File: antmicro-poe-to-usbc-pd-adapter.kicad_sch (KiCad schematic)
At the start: 0 parts

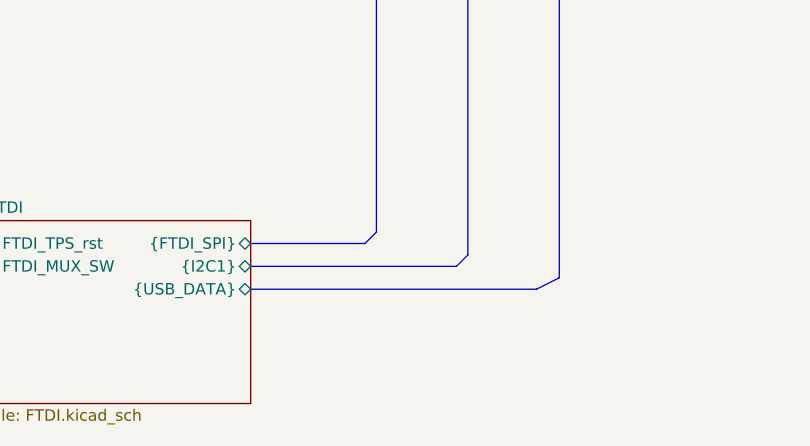
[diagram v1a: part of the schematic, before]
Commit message: [#62835] Tacle ERC problems, add PWR flags
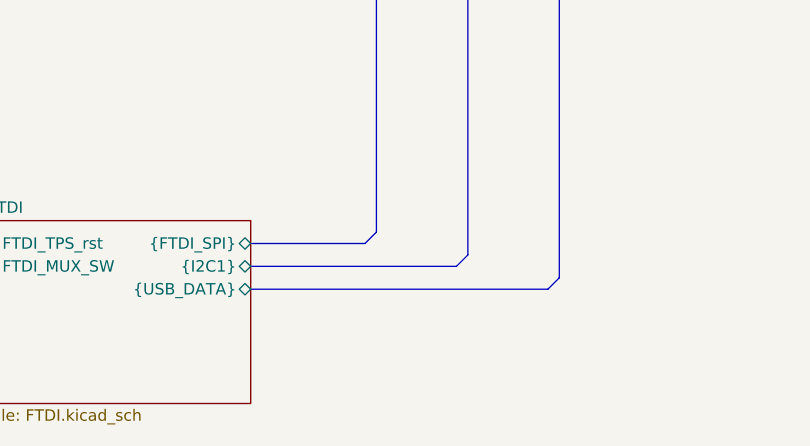
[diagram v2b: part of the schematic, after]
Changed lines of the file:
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@@
   (junction (at 232.41 111.76) (diameter 0) (color 0 0 0 0)
-  )
-  (bus (pts (xy 208.28 166.37) (xy 240.03 166.37))
-    (stroke (width 0) (type default))
   )
   (wire (pts (xy 173.99 124.46) (xy 179.07 124.46))
@@
     (stroke (width 0) (type default))
   )
-  (bus (pts (xy 240.03 166.37) (xy 242.57 165.1))
+  (bus (pts (xy 241.3 166.37) (xy 242.57 165.1))
     (stroke (width 0) (type default))
   )
@@
     (stroke (width 0) (type default))
   )
+  (bus (pts (xy 208.28 166.37) (xy 241.3 166.37))
+    (stroke (width 0) (type default))
+  )

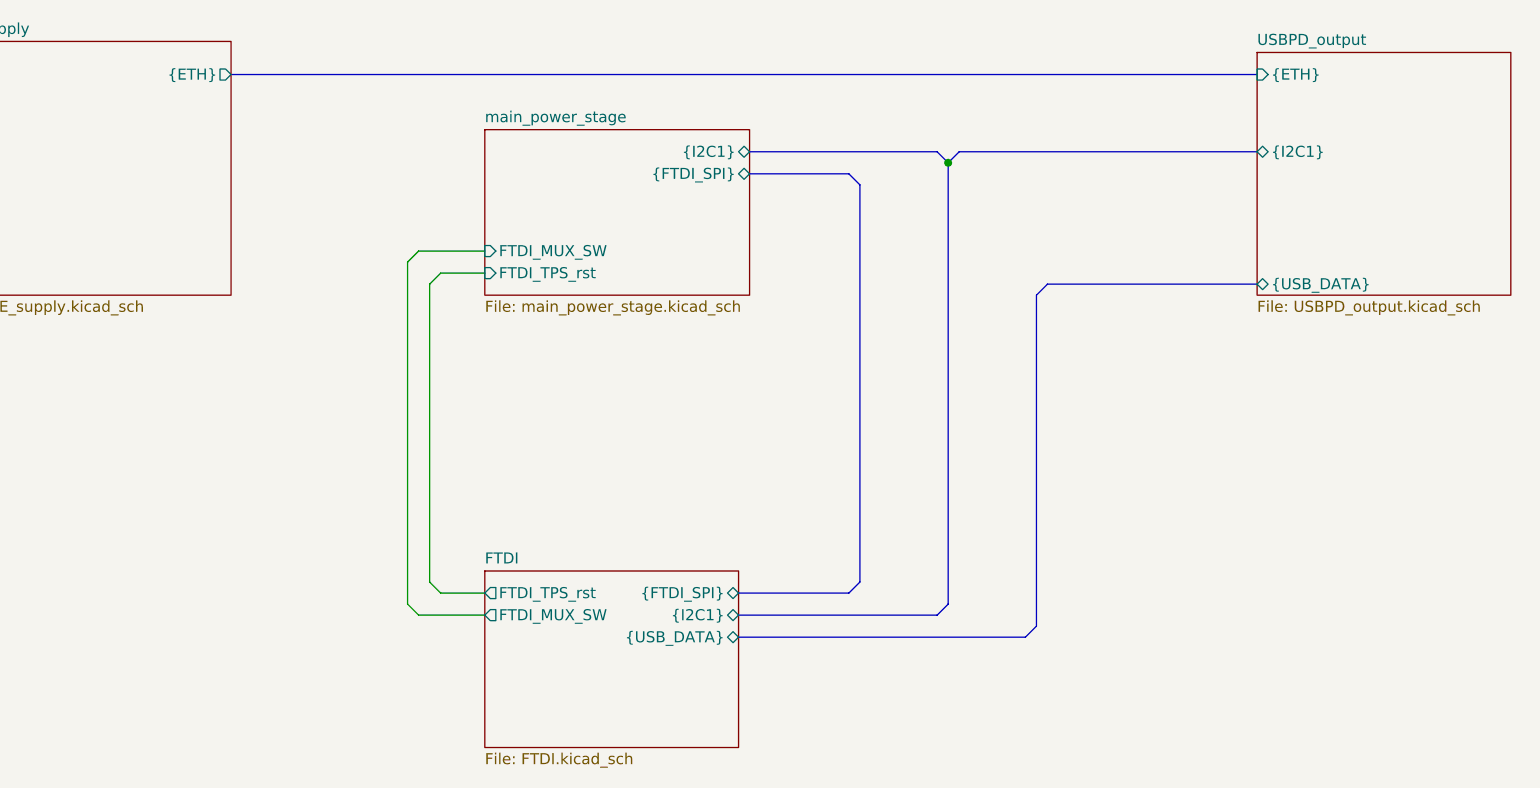
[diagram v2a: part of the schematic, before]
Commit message: [#62835] PoE to USB-C PD Review Rev.1.0.0 correct points 1,3,4,6,7,11
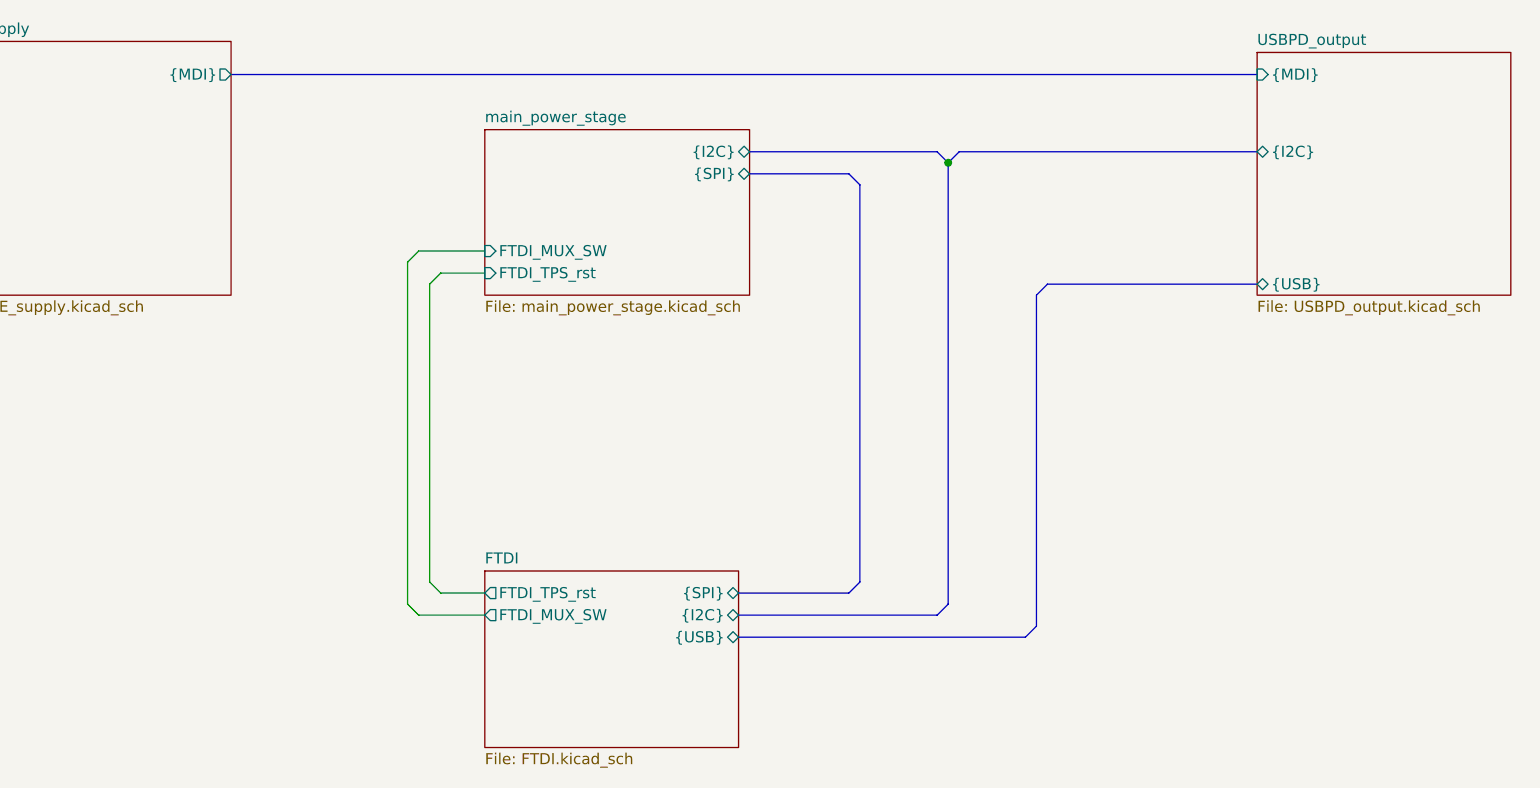
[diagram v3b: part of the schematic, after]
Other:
- sheet FTDI ports: added {I2C}, {SPI}, {USB}; removed {FTDI_SPI}, {I2C1}, {USB_DATA}
- sheet PoE_supply ports: added {MDI}; removed {ETH}
- sheet USBPD_output ports: added {I2C}, {MDI}, {USB}; removed {ETH}, {I2C1}, {USB_DATA}
- sheet main_power_stage ports: added {I2C}, {SPI}; removed {FTDI_SPI}, {I2C1}
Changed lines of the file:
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@@
     (company "Antmicro ltd.")
   )
-  (bus_alias "Buck_FB" (members "FB1" "FB2" "FB3" "FB4"))
-  (bus_alias "CC" (members "CC1" "CC2"))
-  (bus_alias "FLASH_SPI" (members "FLASH_SCK" "FLASH_SDO" "FLASH_SDI" "FLASH_CS"))
-  (bus_alias "POE_PWR" (members "VC1" "VC2" "VC3" "VC4"))
   (junction (at 232.41 111.76) (diameter 0) (color 0 0 0 0)
   )
@@
       (effects (font (size 1.27 1.27)) (justify left))
     )
-    (pin "{I2C1}" bidirectional (at 209.55 110.49 0)
+    (pin "{I2C}" bidirectional (at 209.55 110.49 0)
       (effects (font (size 1.27 1.27)) (justify right))
     )
@@
       (effects (font (size 1.27 1.27)) (justify left))
     )
-    (pin "{FTDI_SPI}" bidirectional (at 209.55 113.03 0)
+    (pin "{SPI}" bidirectional (at 209.55 113.03 0)
       (effects (font (size 1.27 1.27)) (justify right))
     )
@@
       (effects (font (size 1.27 1.27)) (justify left top))
     )
-    (pin "{USB_DATA}" bidirectional (at 267.97 125.73 180)
+    (pin "{USB}" bidirectional (at 267.97 125.73 180)
       (effects (font (size 1.27 1.27)) (justify left))
     )
-    (pin "{I2C1}" bidirectional (at 267.97 110.49 180)
+    (pin "{I2C}" bidirectional (at 267.97 110.49 180)
       (effects (font (size 1.27 1.27)) (justify left))
     )
-    (pin "{ETH}" input (at 267.97 101.6 180)
+    (pin "{MDI}" input (at 267.97 101.6 180)
       (effects (font (size 1.27 1.27)) (justify left))
     )
@@
       (effects (font (size 1.27 1.27)) (justify left top))
     )
-    (pin "{USB_DATA}" bidirectional (at 208.28 166.37 0)
+    (pin "{USB}" bidirectional (at 208.28 166.37 0)
       (effects (font (size 1.27 1.27)) (justify right))
     )
-    (pin "{FTDI_SPI}" bidirectional (at 208.28 161.29 0)
+    (pin "{SPI}" bidirectional (at 208.28 161.29 0)
       (effects (font (size 1.27 1.27)) (justify right))
     )
@@
       (effects (font (size 1.27 1.27)) (justify left))
     )
-    (pin "{I2C1}" bidirectional (at 208.28 163.83 0)
+    (pin "{I2C}" bidirectional (at 208.28 163.83 0)
       (effects (font (size 1.27 1.27)) (justify right))
     )
@@
       (effects (font (size 1.27 1.27)) (justify left top))
     )
-    (pin "{ETH}" output (at 149.86 101.6 0)
+    (pin "{MDI}" output (at 149.86 101.6 0)
       (effects (font (size 1.27 1.27)) (justify right))
     )

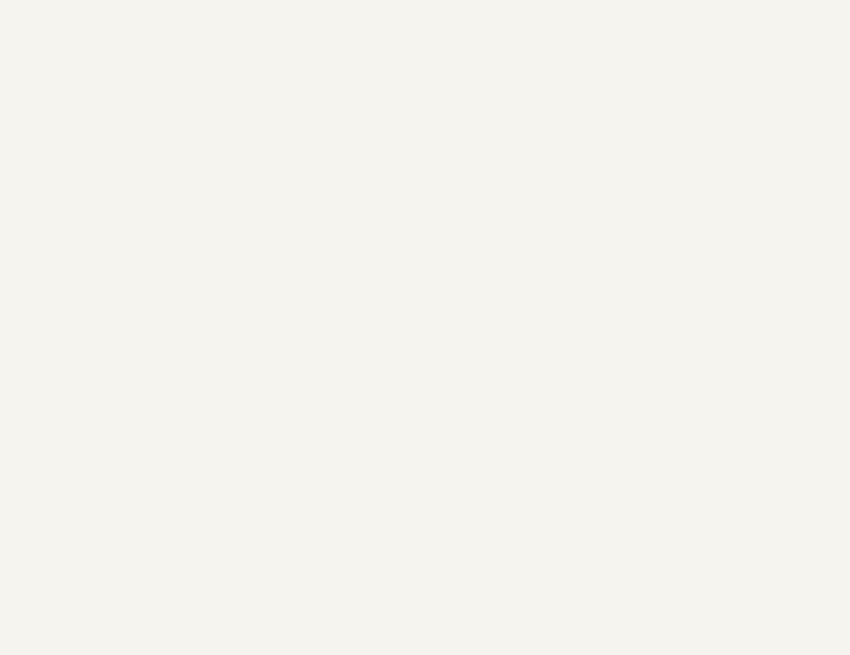
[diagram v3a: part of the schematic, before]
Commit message: [#63274] Add testpoints, improve silcscreen
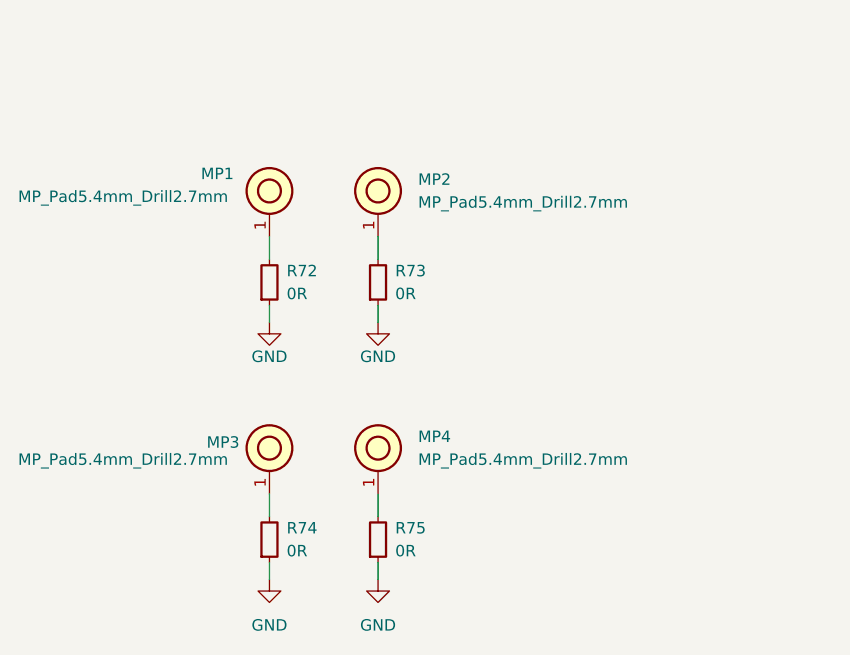
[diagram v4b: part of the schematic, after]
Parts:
- added MP1, MP2, MP3, MP4: MP_Pad5.4mm_Drill2.7mm, antmicro-footprints:MP_Pad5.4mm_Drill2.7mm, symbol antmicroMechanicalParts:MP_Pad5.4mm_Drill2.7mm
- added R72, R73, R74, R75: R_0R_0402, antmicro-footprints:R_0402_1005Metric, symbol antmicroResistors0402:R_0R_0402
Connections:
- new net: MP4.1, R75.2
- new net: MP3.1, R74.2
- new net: MP1.1, R72.2
- new net: MP2.1, R73.2
- new net GND: R72.1, R73.1, R74.1, R75.1

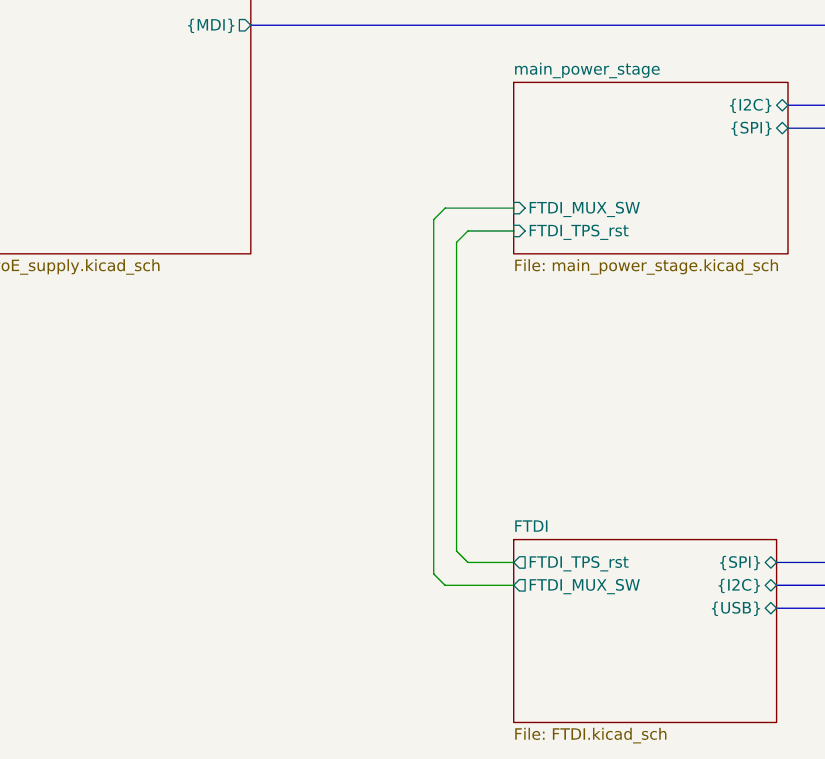
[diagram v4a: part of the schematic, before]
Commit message: [#63274] Add optocouplers for ETH diode, TPS65987D HRESET
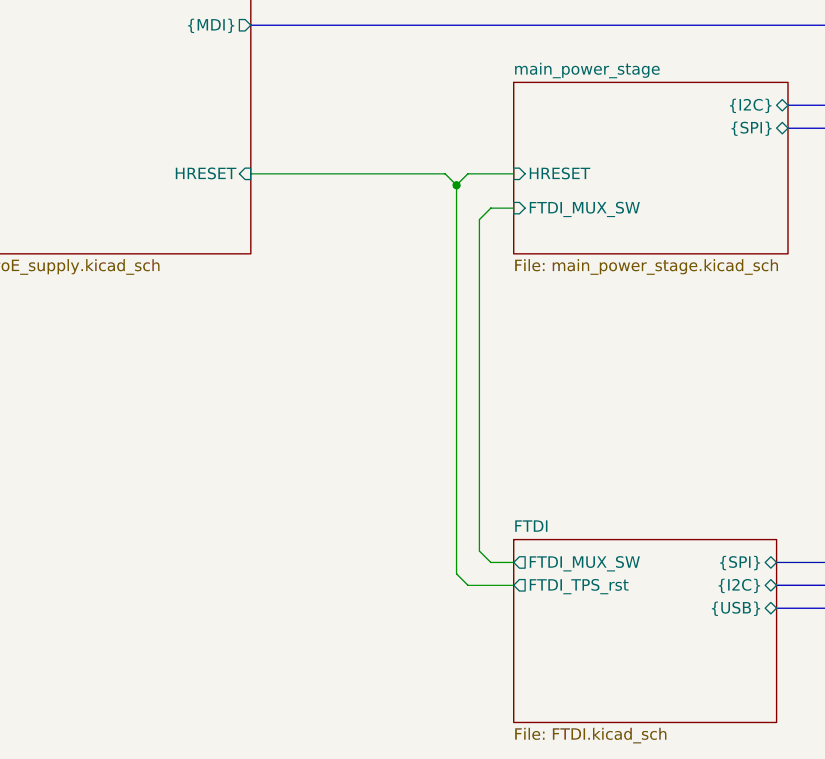
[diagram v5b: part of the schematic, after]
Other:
- sheet PoE_supply ports: added HRESET; removed none
- sheet main_power_stage ports: added HRESET; removed FTDI_TPS_rst
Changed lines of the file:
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@@
     (comment 1 "www.antmicro.com")
   )
+  (junction (at 172.72 119.38) (diameter 0) (color 0 0 0 0)
+  )
   (junction (at 232.41 111.76) (diameter 0) (color 0 0 0 0)
   )
-  (wire (pts (xy 173.99 124.46) (xy 179.07 124.46))
+  (wire (pts (xy 149.86 118.11) (xy 171.45 118.11))
     (stroke (width 0) (type default))
   )
@@
     (stroke (width 0) (type default))
   )
-  (wire (pts (xy 171.45 163.83) (xy 179.07 163.83))
+  (wire (pts (xy 176.53 161.29) (xy 179.07 161.29))
     (stroke (width 0) (type default))
   )
@@
     (stroke (width 0) (type default))
   )
+  (wire (pts (xy 172.72 119.38) (xy 172.72 162.56))
+    (stroke (width 0) (type default))
+  )
   (wire (pts (xy 60.96 248.285) (xy 60.96 250.19))
     (stroke (width 0) (type default))
@@
     (stroke (width 0) (type default))
   )
-  (wire (pts (xy 172.72 125.73) (xy 173.99 124.46))
-    (stroke (width 0) (type default))
-  )
-  (wire (pts (xy 171.45 163.83) (xy 170.18 162.56))
-    (stroke (width 0) (type default))
-  )
-  (wire (pts (xy 170.18 123.19) (xy 170.18 162.56))
+  (wire (pts (xy 176.53 161.29) (xy 175.26 160.02))
+    (stroke (width 0) (type default))
+  )
+  (wire (pts (xy 175.26 123.19) (xy 175.26 160.02))
+    (stroke (width 0) (type default))
+  )
+  (wire (pts (xy 172.72 119.38) (xy 171.45 118.11))
     (stroke (width 0) (type default))
   )
@@
     (stroke (width 0) (type default))
   )
-  (wire (pts (xy 173.99 161.29) (xy 179.07 161.29))
-    (stroke (width 0) (type default))
-  )
-  (wire (pts (xy 172.72 125.73) (xy 172.72 160.02))
+  (wire (pts (xy 173.99 118.11) (xy 179.07 118.11))
     (stroke (width 0) (type default))
   )
@@
     (stroke (width 0) (type default))
   )
-  (wire (pts (xy 173.99 161.29) (xy 172.72 160.02))
+  (wire (pts (xy 173.99 163.83) (xy 172.72 162.56))
+    (stroke (width 0) (type default))
+  )
+  (wire (pts (xy 173.99 163.83) (xy 179.07 163.83))
     (stroke (width 0) (type default))
   )
@@
     (stroke (width 0) (type default))
   )
-  (wire (pts (xy 170.18 123.19) (xy 171.45 121.92))
+  (wire (pts (xy 172.72 119.38) (xy 173.99 118.11))
+    (stroke (width 0) (type default))
+  )
+  (wire (pts (xy 175.26 123.19) (xy 176.53 121.92))
     (stroke (width 0) (type default))
   )
@@
     (stroke (width 0) (type default))
   )
-  (wire (pts (xy 171.45 121.92) (xy 179.07 121.92))
+  (wire (pts (xy 176.53 121.92) (xy 179.07 121.92))
     (stroke (width 0) (type default))
   )
@@
       (effects (font (size 1.27 1.27)) (justify left top))
     )
-    (pin "FTDI_TPS_rst" input (at 179.07 124.46 180)
-      (effects (font (size 1.27 1.27)) (justify left))
-    )
     (pin "{I2C}" bidirectional (at 209.55 110.49 0)
       (effects (font (size 1.27 1.27)) (justify right))
@@
     (pin "{SPI}" bidirectional (at 209.55 113.03 0)
       (effects (font (size 1.27 1.27)) (justify right))
+    )
+    (pin "HRESET" input (at 179.07 118.11 180)
+      (effects (font (size 1.27 1.27)) (justify left))
     )
     (instances
@@
       (effects (font (size 1.27 1.27)) (justify right))
     )
-    (pin "FTDI_MUX_SW" output (at 179.07 163.83 180)
+    (pin "FTDI_MUX_SW" output (at 179.07 161.29 180)
       (effects (font (size 1.27 1.27)) (justify left))
     )
-    (pin "FTDI_TPS_rst" output (at 179.07 161.29 180)
+    (pin "FTDI_TPS_rst" output (at 179.07 163.83 180)
       (effects (font (size 1.27 1.27)) (justify left))
     )
@@
       (effects (font (size 1.27 1.27)) (justify right))
     )
+    (pin "HRESET" input (at 149.86 118.11 0)
+      (effects (font (size 1.27 1.27)) (justify right))
+    )

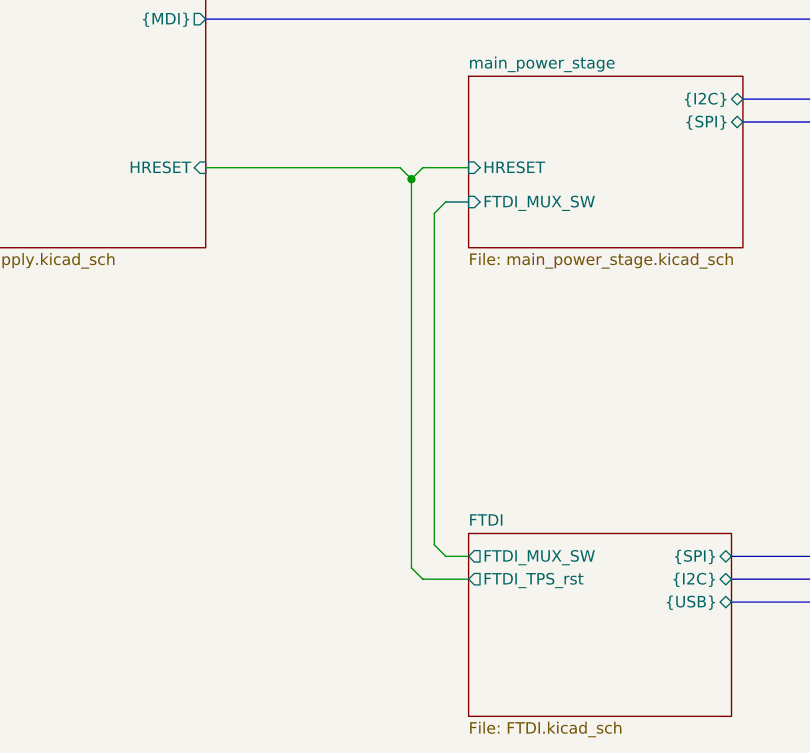
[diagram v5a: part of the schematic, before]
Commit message: [#63274] Remove one optocoupler, add components to PCB, route PCB
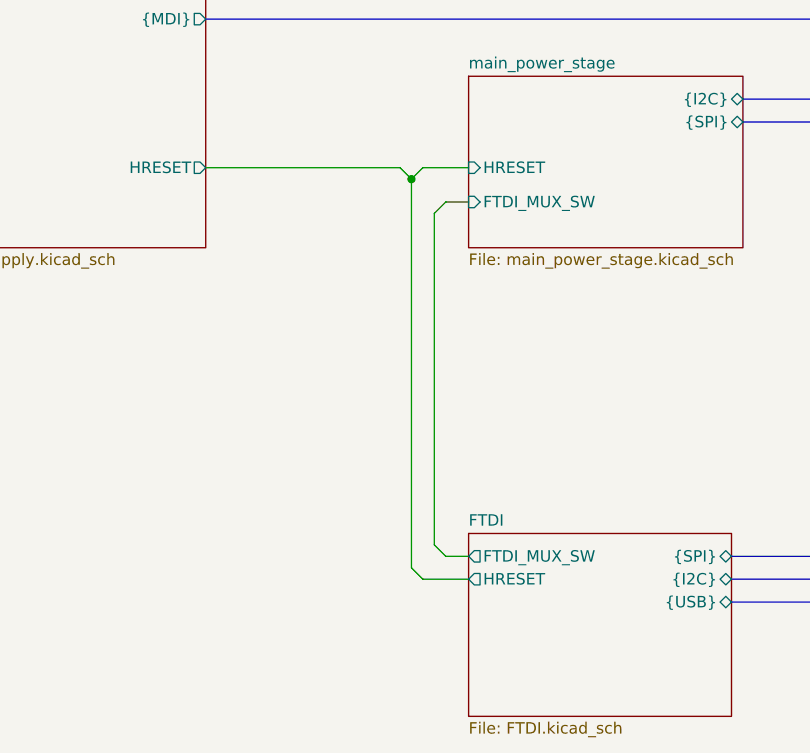
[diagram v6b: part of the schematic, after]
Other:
- sheet FTDI ports: added HRESET; removed FTDI_TPS_rst
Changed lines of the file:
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@@
-      (effects (font (size 1.27 1.27)) (justify left))
-    )
-    (pin "FTDI_TPS_rst" output (at 179.07 163.83 180)
       (effects (font (size 1.27 1.27)) (justify left))
     )
     (pin "{I2C}" bidirectional (at 208.28 163.83 0)
       (effects (font (size 1.27 1.27)) (justify right))
+    )
+    (pin "HRESET" output (at 179.07 163.83 180)
+      (effects (font (size 1.27 1.27)) (justify left))
     )
     (instances
@@
       (effects (font (size 1.27 1.27)) (justify right))
     )
-    (pin "HRESET" input (at 149.86 118.11 0)
+    (pin "HRESET" output (at 149.86 118.11 0)
       (effects (font (size 1.27 1.27)) (justify right))
     )

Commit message: [#64013] Prepare production fixes
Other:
- company: Antmicro ltd. -> Antmicro Ltd.
- moved on the sheet: MP1, MP3, MP4, R72, R74, R75
